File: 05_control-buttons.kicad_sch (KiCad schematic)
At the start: 0 parts

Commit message: Adds SD card connector, control buttons and debug headers
Signed-off-by: Anna-Lena Marx <anna-lena.marx@web.de>
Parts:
- added R5, R6, R7: 4.7k, Resistor_SMD:R_1206_3216Metric_Pad1.30x1.75mm_HandSolder, symbol Device:R
- added SW1, SW2, SW3: SW_Push, Button_Switch_THT:SW_PUSH_6mm_H4.3mm, symbol Switch:SW_Push
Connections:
- new net +3.3V: R5.2, R6.2, R7.1
- new net BTN_1: R5.1, SW1.2
- new net BTN_2: R6.1, SW2.2
- new net BTN_3: R7.2, SW3.2
- new net GND: SW1.1, SW2.1, SW3.1

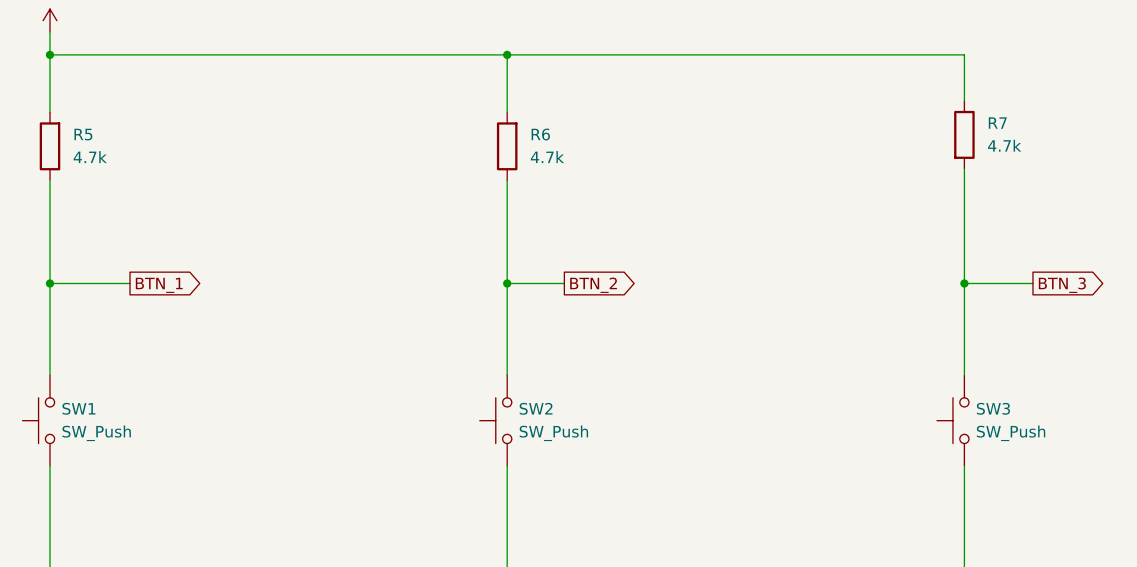
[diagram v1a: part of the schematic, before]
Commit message: Add EPD Driver Circuit
Signed-off-by: Anna-Lena Marx <anna-lena.marx@web.de>
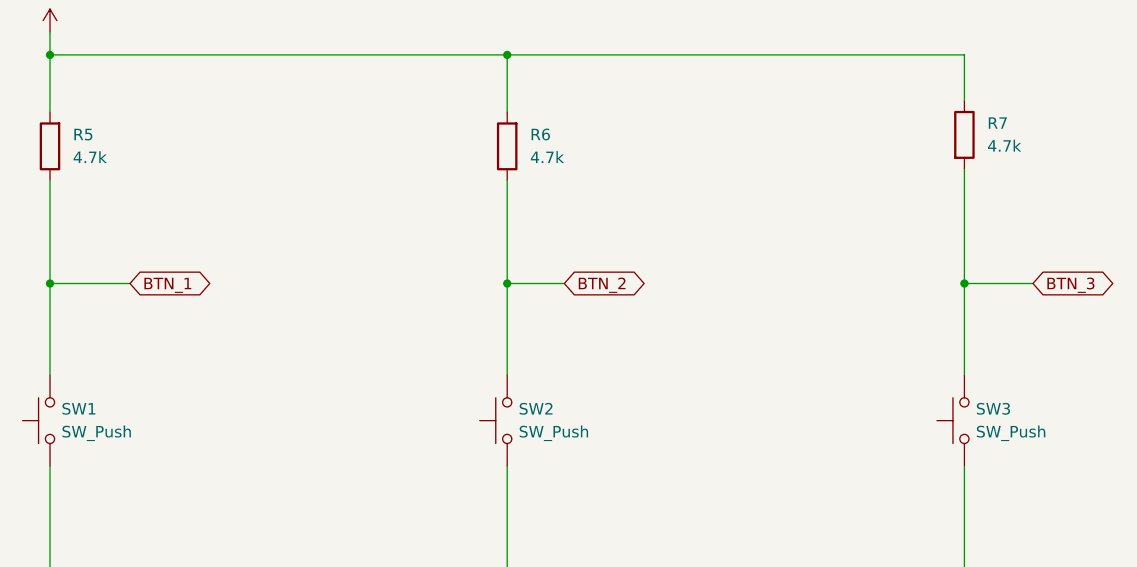
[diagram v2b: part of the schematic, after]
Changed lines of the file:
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@@
 	)
 	(global_label "BTN_3"
-		(shape output)
+		(shape bidirectional)
 		(at 210.82 81.28 0)
 		(fields_autoplaced yes)
@@
 		)
 		(property "Intersheetrefs" "${INTERSHEET_REFS}"
-			(at 219.5504 81.28 0)
+			(at 220.6617 81.28 0)
 			(effects
 				(font
@@
 	)
 	(global_label "BTN_1"
-		(shape output)
+		(shape bidirectional)
 		(at 110.49 81.28 0)
 		(fields_autoplaced yes)
@@
 		)
 		(property "Intersheetrefs" "${INTERSHEET_REFS}"
-			(at 119.2204 81.28 0)
+			(at 120.3317 81.28 0)
 			(effects
 				(font
@@
 	)
 	(global_label "BTN_2"
-		(shape output)
+		(shape bidirectional)
 		(at 158.75 81.28 0)
 		(fields_autoplaced yes)
@@
 		)
 		(property "Intersheetrefs" "${INTERSHEET_REFS}"
-			(at 167.4804 81.28 0)
+			(at 168.5917 81.28 0)
 			(effects
 				(font

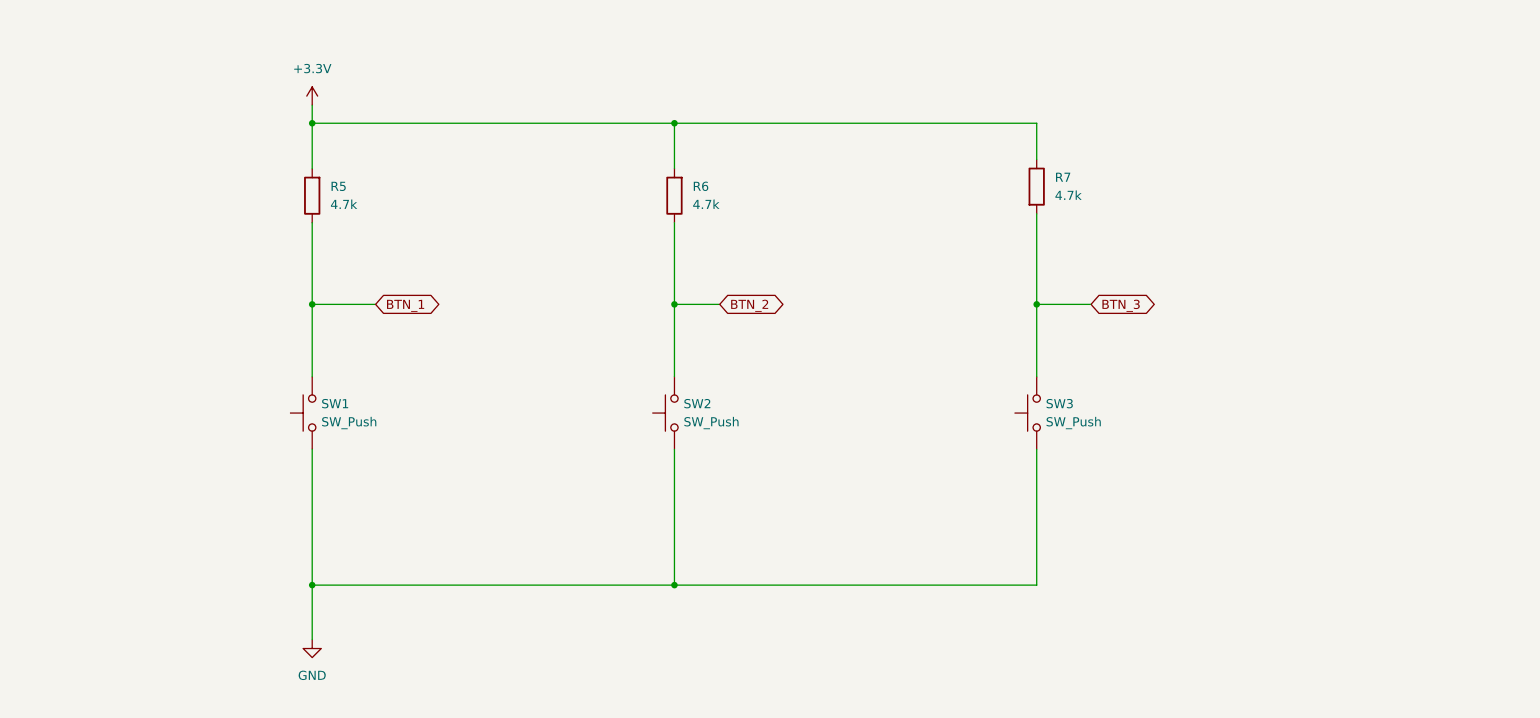
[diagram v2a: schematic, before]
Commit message: Added USB-C, Battery Charging andOn/Off
Signed-off-by: Anna-Lena Marx <anna-lena.marx@web.de>
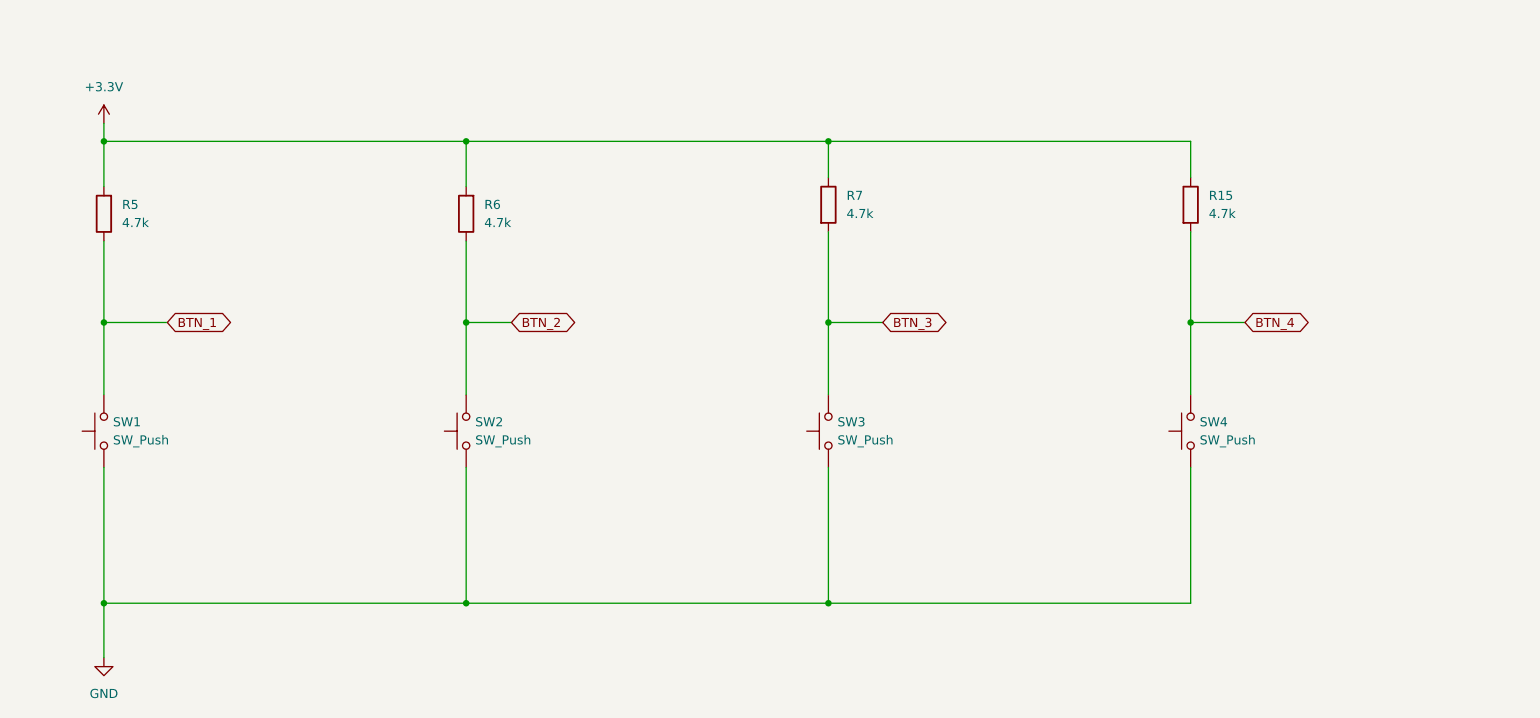
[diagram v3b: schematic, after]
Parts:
- added R15: 4.7k, Resistor_SMD:R_1206_3216Metric_Pad1.30x1.75mm_HandSolder, symbol Device:R
- added SW4: SW_Push, Button_Switch_THT:SW_PUSH-12mm, symbol Switch:SW_Push
- SW1, SW2, SW3: footprint Button_Switch_THT:SW_PUSH_6mm_H4.3mm -> Button_Switch_THT:SW_PUSH-12mm
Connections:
- net +3.3V: now also R15.1
- net GND: now also SW4.1
- new net BTN_4: R15.2, SW4.2
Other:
- moved on the sheet: R5, R6, R7, SW1, SW2, SW3

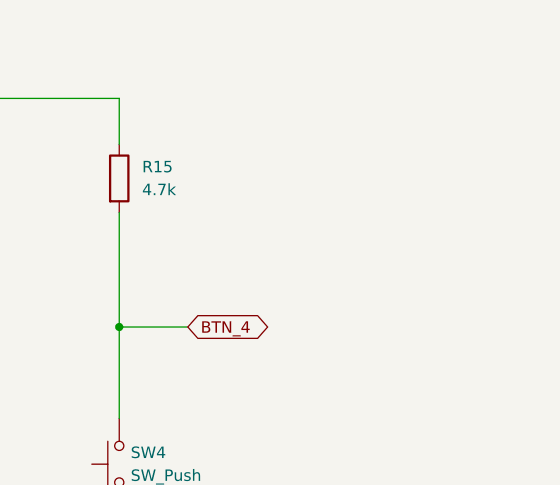
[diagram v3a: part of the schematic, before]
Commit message: Added some more notes, testpoints and rechecked footprints and parts
Signed-off-by: Anna-Lena Marx <anna-lena.marx@web.de>
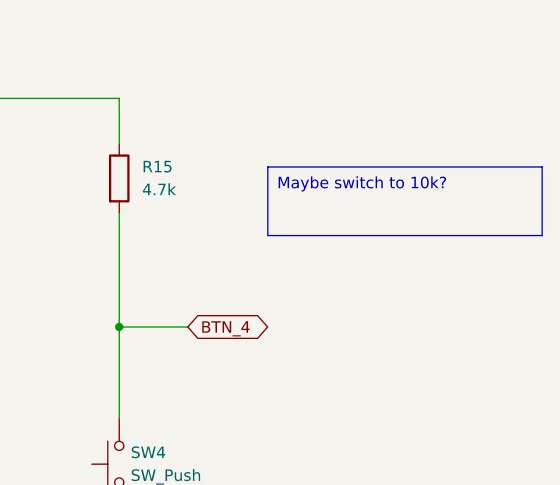
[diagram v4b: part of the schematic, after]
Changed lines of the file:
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@@
+		)
+	)
+	(text_box "Maybe switch to 10k?"
+		(exclude_from_sim no)
+		(at 241.3 66.04 0)
+		(size 30.48 7.62)
+		(stroke
+			(width 0)
+			(type default)
+		)
+		(fill
+			(type none)
+		)
+		(effects
+			(font
+				(size 1.27 1.27)
+			)
+			(justify left top)
 		)
 	)

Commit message: Changed buttons to smaller ones, updated some comments
Signed-off-by: Anna-Lena Marx <anna-lena.marx@web.de>
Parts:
- SW1, SW2, SW3, SW4: footprint Button_Switch_THT:SW_PUSH-12mm -> Button_Switch_THT:SW_PUSH_6mm
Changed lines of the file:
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@@
 			)
 		)
-		(property "Footprint" "Button_Switch_THT:SW_PUSH-12mm"
+		(property "Footprint" "Button_Switch_THT:SW_PUSH_6mm"
 			(at 118.11 99.06 0)
 			(effects
@@
 			)
 		)
-		(property "Footprint" "Button_Switch_THT:SW_PUSH-12mm"
+		(property "Footprint" "Button_Switch_THT:SW_PUSH_6mm"
 			(at 168.91 99.06 0)
 			(effects
@@
 			)
 		)
-		(property "Footprint" "Button_Switch_THT:SW_PUSH-12mm"
+		(property "Footprint" "Button_Switch_THT:SW_PUSH_6mm"
 			(at 219.71 99.06 0)
 			(effects
@@
 			)
 		)
-		(property "Footprint" "Button_Switch_THT:SW_PUSH-12mm"
+		(property "Footprint" "Button_Switch_THT:SW_PUSH_6mm"
 			(at 67.31 99.06 0)
 			(effects

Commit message: Reordered and rerouted display charge pump part
Signed-off-by: Anna-Lena Marx <anna-lena.marx@web.de>
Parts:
- added C14: 10uF, Capacitor_SMD:C_1206_3216Metric_Pad1.33x1.80mm_HandSolder, symbol Device:C
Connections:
- net +3.3V: now also C14.2
- net GND: now also C14.1
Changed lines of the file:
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@@
+	)
+	(junction
+		(at 72.39 58.42)
+		(diameter 0)
+		(color 0 0 0 0)
 	)
 	(junction
@@
 	)
 	(junction
-		(at 72.39 58.42)
+		(at 72.39 46.99)
 		(diameter 0)
 		(color 0 0 0 0)
@@
 	(wire
 		(pts
+			(xy 72.39 46.99) (xy 72.39 58.42)
+		)
+		(stroke
+			(width 0)
+			(type default)
+		)
+	)
+	(wire
+		(pts
 			(xy 224.79 123.19) (xy 173.99 123.19)
 		)
@@
 	(wire
 		(pts
+			(xy 62.23 46.99) (xy 72.39 46.99)
+		)
+		(stroke
+			(width 0)
+			(type default)
+		)
+	)
+	(wire
+		(pts
 			(xy 123.19 83.82) (xy 129.54 83.82)
 		)
@@
 	(wire
 		(pts
-			(xy 72.39 55.88) (xy 72.39 58.42)
+			(xy 62.23 46.99) (xy 62.23 49.53)
 		)
 		(stroke
@@
 				(justify left)
 				(hide yes)
+			)
+		)
+	)
+	(netclass_flag ""
+		(length 2.54)
+		(shape round)
+		(at 81.28 58.42 0)
+		(fields_autoplaced yes)
+		(effects
+			(font
+				(size 1.27 1.27)
+			)
+			(justify left bottom)
+		)
+		(property "Netclass" "PWR"
+			(at 81.9785 55.88 0)
+			(effects
+				(font
+					(size 1.27 1.27)
+					(italic yes)
+				)
+				(justify left)
+			)
+		)
+	)
+	(symbol
+		(lib_id "Device:C")
+		(at 62.23 53.34 180)
+		(unit 1)
+		(exclude_from_sim no)
+		(in_bom yes)
+		(on_board yes)
+		(dnp no)
+		(fields_autoplaced yes)
+		(property "Reference" "C14"
+			(at 66.04 52.0699 0)
+			(effects
+				(font
+					(size 1.27 1.27)
+				)
+				(justify right)
+			)
+		)
+		(property "Value" "10uF"
+			(at 66.04 54.6099 0)
+			(effects
+				(font
+					(size 1.27 1.27)
+				)
+				(justify right)
+			)
+		)
+		(property "Footprint" "Capacitor_SMD:C_1206_3216Metric_Pad1.33x1.80mm_HandSolder"
+			(at 61.2648 49.53 0)
+			(effects
+				(font
+					(size 1.27 1.27)
+				)
+				(hide yes)
+			)
+		)
+		(property "Datasheet" "~"
+			(at 62.23 53.34 0)
+			(effects
+				(font
+					(size 1.27 1.27)
+				)
+				(hide yes)
+			)
+		)
+		(property "Description" "Unpolarized capacitor"
+			(at 62.23 53.34 0)
+			(effects
+				(font
+					(size 1.27 1.27)
+				)
+				(hide yes)
+			)
+		)
+		(pin "2"
+		)
+		(pin "1"
+		)
+		(instances
+			(project ""
+				(path "/ec954637-2a8b-4662-b4a1-f88107f11cb0/33ac9274-8ec9-4374-b845-560e6893b431"
+					(reference "C14")
+					(unit 1)
+				)
 			)
 		)
@@
 	)
 	(symbol
+		(lib_id "power:GND")
+		(at 62.23 57.15 0)
+		(unit 1)
+		(exclude_from_sim no)
+		(in_bom yes)
+		(on_board yes)
+		(dnp no)
+		(fields_autoplaced yes)
+		(property "Reference" "#PWR033"
+			(at 62.23 63.5 0)
+			(effects
+				(font
+					(size 1.27 1.27)
+				)
+				(hide yes)
+			)
+		)
+		(property "Value" "GND"
+			(at 62.23 62.23 0)
+			(effects
+				(font
+					(size 1.27 1.27)
+				)
+			)
+		)
+		(property "Footprint" ""
+			(at 62.23 57.15 0)
+			(effects
+				(font
+					(size 1.27 1.27)
+				)
+				(hide yes)
+			)
+		)
+		(property "Datasheet" ""
+			(at 62.23 57.15 0)
+			(effects
+				(font
+					(size 1.27 1.27)
+				)
+				(hide yes)
+			)
+		)
+		(property "Description" "Power symbol creates a global label with name \"GND\" , ground"
+			(at 62.23 57.15 0)
+			(effects
+				(font
+					(size 1.27 1.27)
+				)
+				(hide yes)
+			)
+		)
+		(pin "1"
+		)
+		(instances
+			(project ""
+				(path "/ec954637-2a8b-4662-b4a1-f88107f11cb0/33ac9274-8ec9-4374-b845-560e6893b431"
+					(reference "#PWR033")
+					(unit 1)
+				)
+			)
+		)
+	)
+	(symbol
 		(lib_id "Switch:SW_Push")
 		(at 173.99 99.06 90)
@@
 	(symbol
 		(lib_id "power:+3.3V")
-		(at 72.39 55.88 0)
+		(at 72.39 46.99 0)
 		(unit 1)
 		(exclude_from_sim no)
@@
 		(fields_autoplaced yes)
 		(property "Reference" "#PWR05"
-			(at 72.39 59.69 0)
+			(at 72.39 50.8 0)
 			(effects
 				(font
@@
 		)
 		(property "Value" "+3.3V"
-			(at 72.39 50.8 0)
+			(at 72.39 41.91 0)
 			(effects
 				(font
@@
 		)
 		(property "Footprint" ""
-			(at 72.39 55.88 0)
+			(at 72.39 46.99 0)
 			(effects
 				(font
@@
 		)
 		(property "Datasheet" ""
-			(at 72.39 55.88 0)
+			(at 72.39 46.99 0)
 			(effects
 				(font
@@
 		)
 		(property "Description" "Power symbol creates a global label with name \"+3.3V\""
-			(at 72.39 55.88 0)
-			(effects
-				(font
+			(at 72.39 46.99 0)
+			(effects
+				(font
